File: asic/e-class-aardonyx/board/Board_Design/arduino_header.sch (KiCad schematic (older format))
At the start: 31 parts, among them J10 Conn_1x6_F, J11 Conn_1x6_F, J12 Conn_1x3_M, J13 Conn_1x8_F, J14 Conn_1x6_F, J15 Conn_1x10, J16 Conn_1x8_F, J7 Conn_1x4, J8 Conn_1x3_M, J9 Conn_1x8, U5 CAT24M01WI-GT3, U6 IS25LP256x-xM, U7 ADC108S102CIMTX, U8 LSF0108PWR, U9 LSF0108PWR

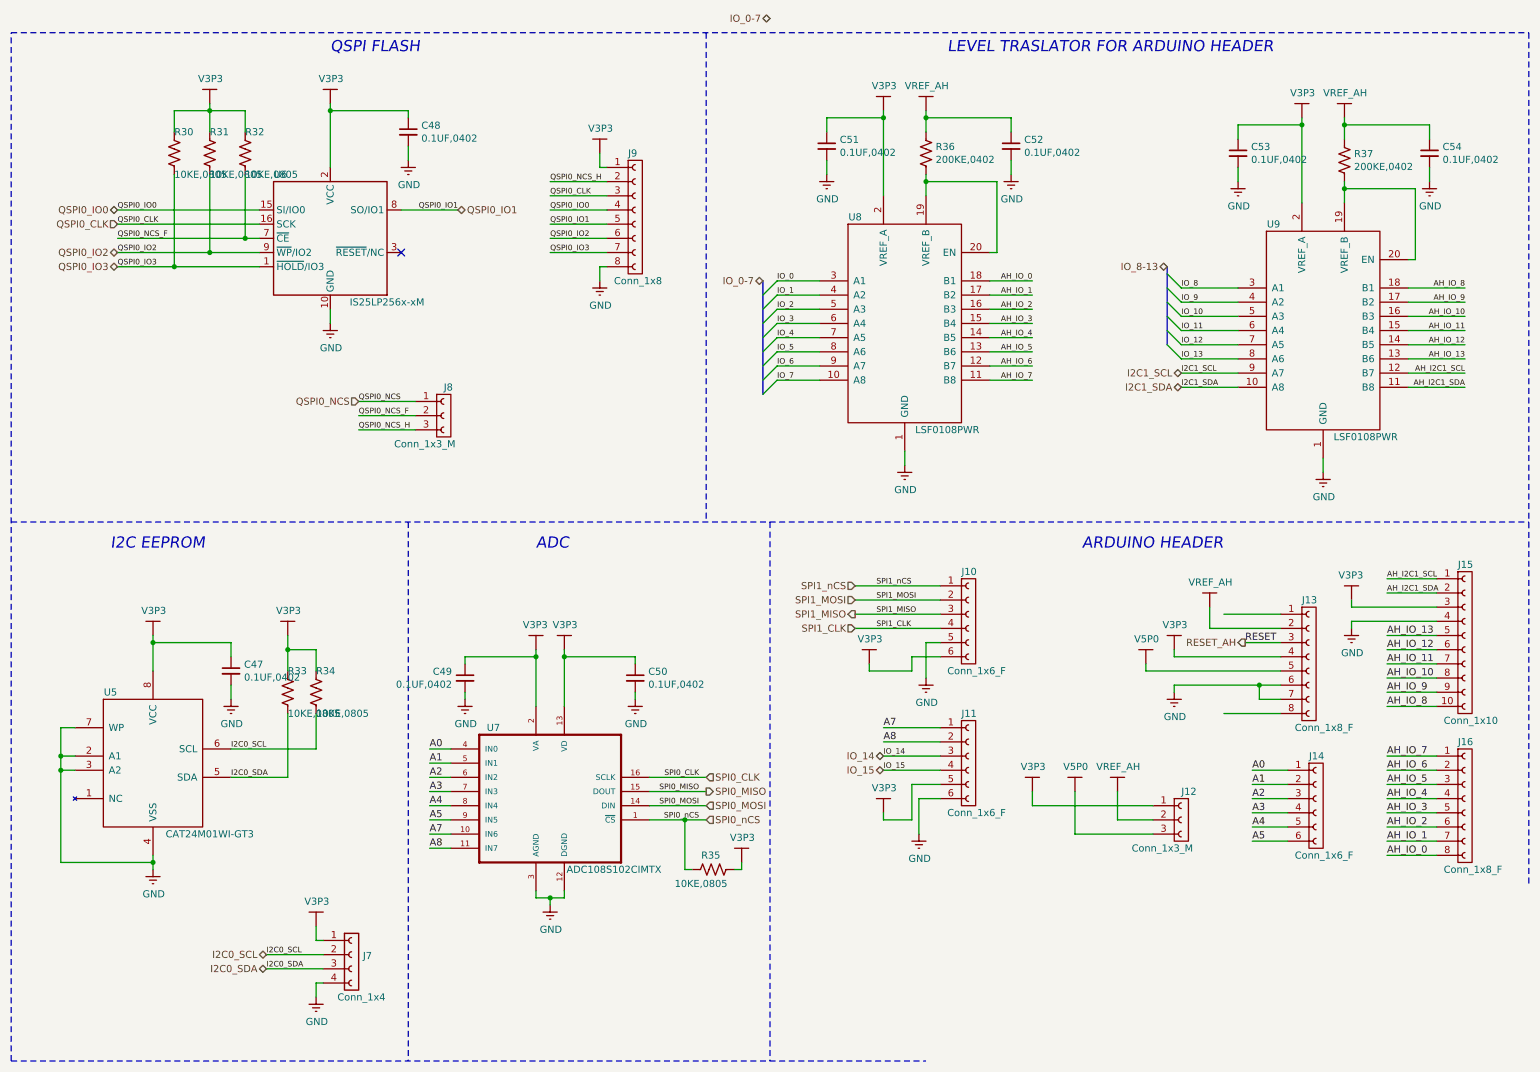
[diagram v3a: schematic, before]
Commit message: updated commented pending schematic
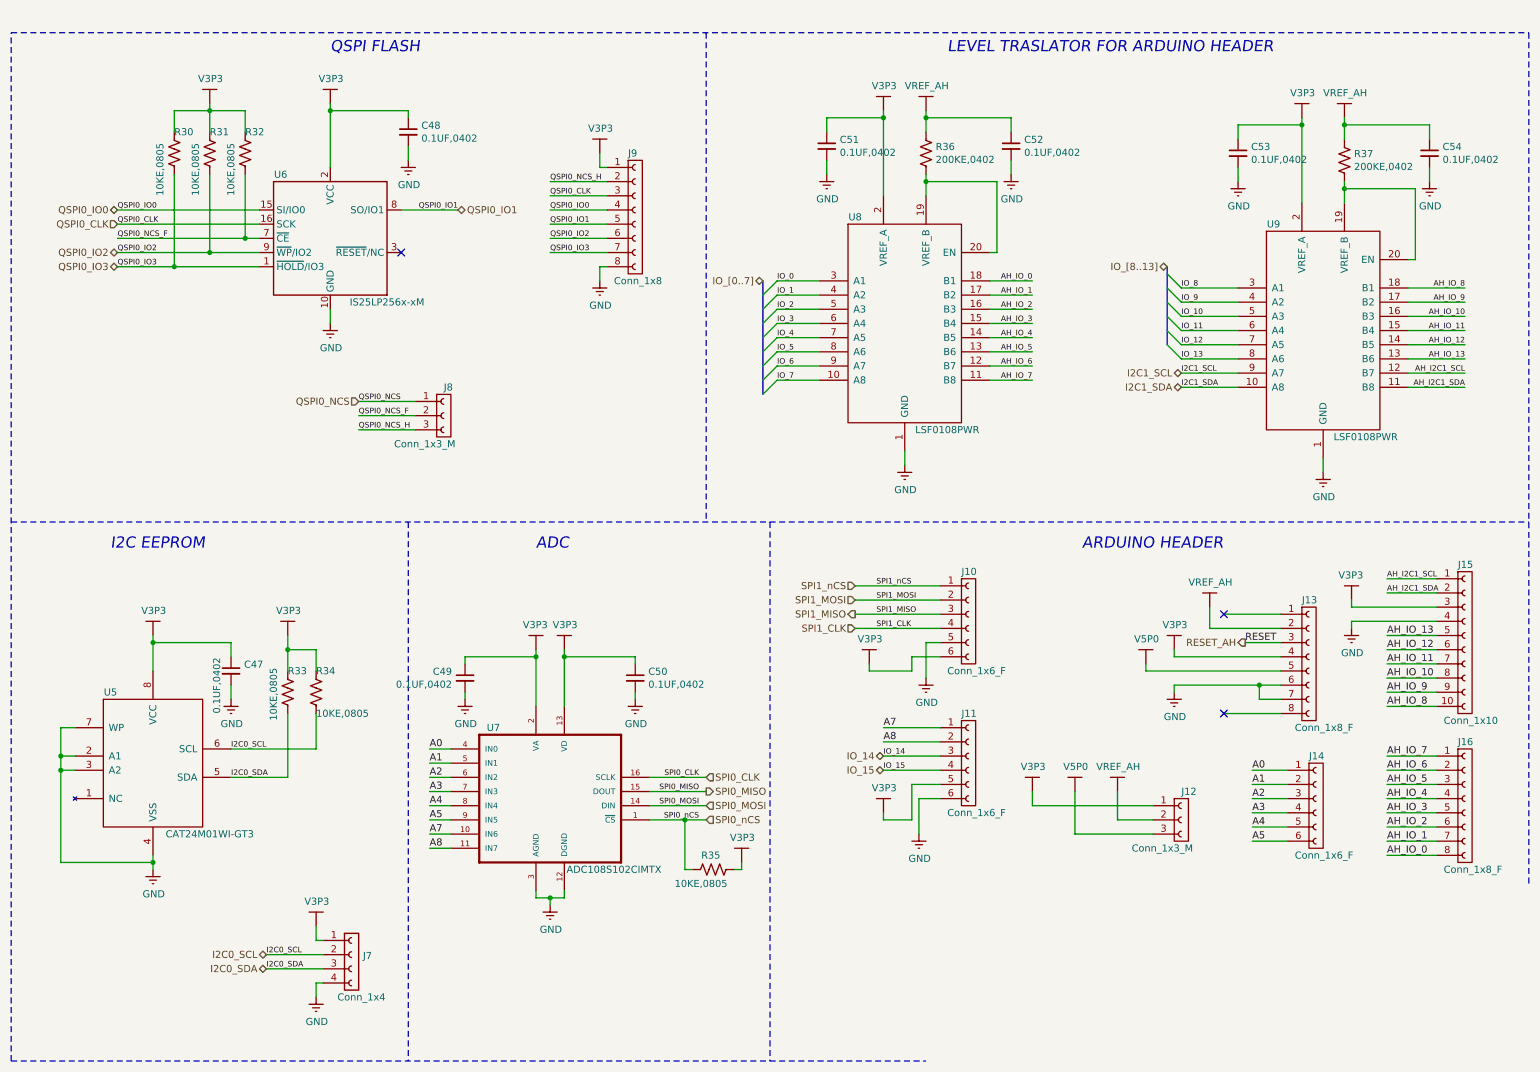
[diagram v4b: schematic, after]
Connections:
- no-connect marks 1 -> 3
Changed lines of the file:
@@
-	1    0    0    -1
-$EndComp
-$Comp
-L Aardonyx-rescue:GND-aardonyx #PWR092
-U 1 1 5E2602C3
-P 10500 1550
-F 0 "#PWR092" H 10500 1300 50  0001 C CNN
-F 1 "GND" H 10505 1377 50  0000 C CNN
-F 2 "" H 10500 1550 50  0001 C CNN
-F 3 "" H 10500 1550 50  0001 C CNN
-	1    10500 1550
 	1    0    0    -1
 $EndComp
@@
 	1    0    0    -1
 $EndComp
-$Comp
-L Aardonyx-rescue:GND-aardonyx #PWR086
-U 1 1 5E266919
-P 9150 1550
-F 0 "#PWR086" H 9150 1300 50  0001 C CNN
-F 1 "GND" H 9155 1377 50  0000 C CNN
-F 2 "" H 9150 1550 50  0001 C CNN
-F 3 "" H 9150 1550 50  0001 C CNN
-	1    9150 1550
-	1    0    0    -1
-$EndComp
 Wire Wire Line
 	9150 1450 9150 1550
@@
 P 2150 1350
 F 0 "R32" H 2150 1500 50  0000 L CNN
-F 1 "10KE,0805" H 2150 1200 50  0000 L CNN
+F 1 "10KE,0805" V 2050 1050 50  0000 L CNN
 F 2 "" V 2190 1340 50  0001 C CNN
 F 3 "https://www.digikey.in/product-detail/en/yageo/RC0805FR-0710KL/311-10-0KCRCT-ND/730482" H 2150 1350 50  0001 C CNN
@@
 P 1650 1350
 F 0 "R30" H 1650 1500 50  0000 L CNN
-F 1 "10KE,0805" H 1650 1200 50  0000 L CNN
+F 1 "10KE,0805" V 1550 1050 50  0000 L CNN
 F 2 "" V 1690 1340 50  0001 C CNN
 F 3 "https://www.digikey.in/product-detail/en/yageo/RC0805FR-0710KL/311-10-0KCRCT-ND/730482" H 1650 1350 50  0001 C CNN
@@
 P 1900 1350
 F 0 "R31" H 1900 1500 50  0000 L CNN
-F 1 "10KE,0805" H 1900 1200 50  0000 L CNN
+F 1 "10KE,0805" V 1800 1050 50  0000 L CNN
 F 2 "" V 1940 1340 50  0001 C CNN
 F 3 "https://www.digikey.in/product-detail/en/yageo/RC0805FR-0710KL/311-10-0KCRCT-ND/730482" H 1900 1350 50  0001 C CNN
@@
 P 2050 5000
 F 0 "C47" H 2142 5046 50  0000 L CNN
-F 1 "0.1UF,0402" H 2142 4955 50  0000 L CNN
+F 1 "0.1UF,0402" V 1950 4700 50  0000 L CNN
 F 2 "" H 2050 5000 50  0001 C CNN
 F 3 "https://www.digikey.in/product-detail/en/avx-corporation/04023C104JAT2A/478-10050-1-ND/6564273" H 2050 5000 50  0001 C CNN
@@
 P 2450 5150
 F 0 "R33" H 2450 5300 50  0000 L CNN
-F 1 "10KE,0805" H 2450 5000 50  0000 L CNN
+F 1 "10KE,0805" V 2350 4950 50  0000 L CNN
 F 2 "" V 2490 5140 50  0001 C CNN
 F 3 "https://www.digikey.in/product-detail/en/yageo/RC0805FR-0710KL/311-10-0KCRCT-ND/730482" H 2450 5150 50  0001 C CNN
@@
 Entry Wire Line
 	5800 3050 5900 2950
-Text HLabel 5850 400  0    50   BiDi ~ 0
-IO_0-7
 Wire Wire Line
 	9150 2300 8750 2300
@@
 	8750 2800 8650 2700
 Text HLabel 8650 2150 0    50   BiDi ~ 0
-IO_8-13
+IO_[8..13]
 Text HLabel 8750 2900 0    50   BiDi ~ 0
 I2C1_SCL
@@
 	10550 5250 10200 5250
 Text HLabel 5800 2250 0    50   BiDi ~ 0
-IO_0-7
+IO_[0..7]
 Text Label 3450 6150 0    50   ~ 0
 A7
@@
 	4200 4850 4200 4900
 Connection ~ 4200 4900
+NoConn ~ 9050 4600
+NoConn ~ 9050 5300
+$Comp
+L Aardonyx-rescue:GND-skt32e_asic #PWR0145
+U 1 1 5EE696CA
+P 9150 1550
+F 0 "#PWR0145" H 9150 1300 50  0001 C CNN
+F 1 "GND" H 9155 1377 50  0000 C CNN
+F 2 "" H 9150 1550 50  0001 C CNN
+F 3 "" H 9150 1550 50  0001 C CNN
+	1    9150 1550
+	1    0    0    -1
+$EndComp
+$Comp
+L Aardonyx-rescue:GND-skt32e_asic #PWR0146
+U 1 1 5EE6C80F
+P 10500 1550
+F 0 "#PWR0146" H 10500 1300 50  0001 C CNN
+F 1 "GND" H 10505 1377 50  0000 C CNN
+F 2 "" H 10500 1550 50  0001 C CNN
+F 3 "" H 10500 1550 50  0001 C CNN
+	1    10500 1550
+	1    0    0    -1
+$EndComp
 Wire Bus Line
 	8650 2150 8650 2700

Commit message: updated footprint for netlist
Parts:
- C47, C48, C49, C50, C51, C52, C53, C54: footprint (none) -> Capacitor_SMD:C_0402_1005Metric
- J12, J8: footprint (none) -> Connector:FanPinHeader_1x03_P2.54mm_Vertical
- R30, R31, R32, R33, R34, R35: footprint (none) -> Resistor_SMD:R_0805_2012Metric
- R36, R37: footprint (none) -> Resistor_SMD:R_0402_1005Metric
- U5: footprint (none) -> Package_SO:TSSOP-8_4.4x3mm_P0.65mm
- U7: footprint (none) -> Package_SO:TSSOP-16_4.4x5mm_P0.65mm
- U8, U9: footprint (none) -> Package_SO:TSSOP-20_4.4x6.5mm_P0.65mm
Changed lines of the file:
@@
 EESchema Schematic File Version 4
-LIBS:Aardonyx-cache
-EELAYER 29 0
+EELAYER 30 0
 EELAYER END
 $Descr A4 11693 8268
@@
 F 0 "U5" H 1200 6150 50  0000 C CNN
 F 1 "CAT24M01WI-GT3" H 1900 5150 50  0000 C CNN
-F 2 "" H 1500 5650 50  0001 C CNN
+F 2 "Package_SO:TSSOP-8_4.4x3mm_P0.65mm" H 1500 5650 50  0001 C CNN
 F 3 "https://www.digikey.in/product-detail/en/on-semiconductor/CAT24M01WI-GT3/CAT24M01WI-GT3OSCT-ND/2698362" H 1500 5650 50  0001 C CNN
 F 4 "IC EEPROM 1M I2C 1MHZ 8SOIC" H 1500 5650 50  0001 C CNN "Description"
@@
 F 0 "U9" H 9400 3350 50  0000 C CNN
 F 1 "LSF0108PWR" H 10050 1850 50  0000 C CNN
-F 2 "" H 9750 2600 50  0001 C CNN
+F 2 "Package_SO:TSSOP-20_4.4x6.5mm_P0.65mm" H 9750 2600 50  0001 C CNN
 F 3 "https://www.digikey.in/product-detail/en/texas-instruments/LSF0108PWR/296-37828-1-ND/4876357" H 9750 2600 50  0001 C CNN
 F 4 "IC TRNSLTR BIDIRECTIONAL 20TSSOP" H 9750 2600 50  0001 C CNN "Description"
@@
 F 0 "R36" H 7018 1396 50  0000 L CNN
 F 1 "200KE,0402" H 7018 1305 50  0000 L CNN
-F 2 "" V 6990 1340 50  0001 C CNN
+F 2 "Resistor_SMD:R_0402_1005Metric" V 6990 1340 50  0001 C CNN
 F 3 "https://www.digikey.com/product-detail/en/koa-speer-electronics-inc/RN73H1ETTP2003B25/2019-RN73H1ETTP2003B25CT-ND/9916930" H 6950 1350 50  0001 C CNN
 F 4 " RES 200K OHM 0.1% 1/16W 0402 " H 6950 1350 50  0001 C CNN "Description"
@@
 F 0 "C52" H 7642 1346 50  0000 L CNN
 F 1 "0.1UF,0402" H 7642 1255 50  0000 L CNN
-F 2 "" H 7550 1300 50  0001 C CNN
+F 2 "Capacitor_SMD:C_0402_1005Metric" H 7550 1300 50  0001 C CNN
 F 3 "https://www.digikey.in/product-detail/en/avx-corporation/04023C104JAT2A/478-10050-1-ND/6564273" H 7550 1300 50  0001 C CNN
 F 4 "CAP CER 0.1UF 25V X7R 0402" H 7550 1300 50  0001 C CNN "Description"
@@
 F 0 "R37" H 9968 1446 50  0000 L CNN
 F 1 "200KE,0402" H 9968 1355 50  0000 L CNN
-F 2 "" V 9940 1390 50  0001 C CNN
+F 2 "Resistor_SMD:R_0402_1005Metric" V 9940 1390 50  0001 C CNN
 F 3 "https://www.digikey.com/product-detail/en/koa-speer-electronics-inc/RN73H1ETTP2003B25/2019-RN73H1ETTP2003B25CT-ND/9916930" H 9900 1400 50  0001 C CNN
 F 4 " RES 200K OHM 0.1% 1/16W 0402 " H 9900 1400 50  0001 C CNN "Description"
@@
 F 0 "C53" H 9242 1396 50  0000 L CNN
 F 1 "0.1UF,0402" H 9242 1305 50  0000 L CNN
-F 2 "" H 9150 1350 50  0001 C CNN
+F 2 "Capacitor_SMD:C_0402_1005Metric" H 9150 1350 50  0001 C CNN
 F 3 "https://www.digikey.in/product-detail/en/avx-corporation/04023C104JAT2A/478-10050-1-ND/6564273" H 9150 1350 50  0001 C CNN
 F 4 "CAP CER 0.1UF 25V X7R 0402" H 9150 1350 50  0001 C CNN "Description"
@@
 F 0 "C51" H 6342 1346 50  0000 L CNN
 F 1 "0.1UF,0402" H 6342 1255 50  0000 L CNN
-F 2 "" H 6250 1300 50  0001 C CNN
+F 2 "Capacitor_SMD:C_0402_1005Metric" H 6250 1300 50  0001 C CNN
 F 3 "https://www.digikey.in/product-detail/en/avx-corporation/04023C104JAT2A/478-10050-1-ND/6564273" H 6250 1300 50  0001 C CNN
 F 4 "CAP CER 0.1UF 25V X7R 0402" H 6250 1300 50  0001 C CNN "Description"
@@
 F 0 "U8" H 6450 3300 50  0000 C CNN
 F 1 "LSF0108PWR" H 7100 1800 50  0000 C CNN
-F 2 "" H 6800 2550 50  0001 C CNN
+F 2 "Package_SO:TSSOP-20_4.4x6.5mm_P0.65mm" H 6800 2550 50  0001 C CNN
 F 3 "https://www.digikey.in/product-detail/en/texas-instruments/LSF0108PWR/296-37828-1-ND/4876357" H 6800 2550 50  0001 C CNN
 F 4 "IC TRNSLTR BIDIRECTIONAL 20TSSOP" H 6800 2550 50  0001 C CNN "Description"
@@
 F 0 "C54" H 10592 1396 50  0000 L CNN
 F 1 "0.1UF,0402" H 10592 1305 50  0000 L CNN
-F 2 "" H 10500 1350 50  0001 C CNN
+F 2 "Capacitor_SMD:C_0402_1005Metric" H 10500 1350 50  0001 C CNN
 F 3 "https://www.digikey.in/product-detail/en/avx-corporation/04023C104JAT2A/478-10050-1-ND/6564273" H 10500 1350 50  0001 C CNN
 F 4 "CAP CER 0.1UF 25V X7R 0402" H 10500 1350 50  0001 C CNN "Description"
@@
 F 0 "C48" H 3392 1246 50  0000 L CNN
 F 1 "0.1UF,0402" H 3392 1155 50  0000 L CNN
-F 2 "" H 3300 1200 50  0001 C CNN
+F 2 "Capacitor_SMD:C_0402_1005Metric" H 3300 1200 50  0001 C CNN
 F 3 "https://www.digikey.in/product-detail/en/avx-corporation/04023C104JAT2A/478-10050-1-ND/6564273" H 3300 1200 50  0001 C CNN
 F 4 "CAP CER 0.1UF 25V X7R 0402" H 3300 1200 50  0001 C CNN "Description"
@@
 F 0 "R32" H 2150 1500 50  0000 L CNN
 F 1 "10KE,0805" V 2050 1050 50  0000 L CNN
-F 2 "" V 2190 1340 50  0001 C CNN
+F 2 "Resistor_SMD:R_0805_2012Metric" V 2190 1340 50  0001 C CNN
 F 3 "https://www.digikey.in/product-detail/en/yageo/RC0805FR-0710KL/311-10-0KCRCT-ND/730482" H 2150 1350 50  0001 C CNN
 F 4 "RES SMD 10K OHM 1% 1/8W 0805" H 2150 1350 50  0001 C CNN "Description"
@@
 F 0 "R30" H 1650 1500 50  0000 L CNN
 F 1 "10KE,0805" V 1550 1050 50  0000 L CNN
-F 2 "" V 1690 1340 50  0001 C CNN
+F 2 "Resistor_SMD:R_0805_2012Metric" V 1690 1340 50  0001 C CNN
 F 3 "https://www.digikey.in/product-detail/en/yageo/RC0805FR-0710KL/311-10-0KCRCT-ND/730482" H 1650 1350 50  0001 C CNN
 F 4 "RES SMD 10K OHM 1% 1/8W 0805" H 1650 1350 50  0001 C CNN "Description"
@@
 F 0 "R31" H 1900 1500 50  0000 L CNN
 F 1 "10KE,0805" V 1800 1050 50  0000 L CNN
-F 2 "" V 1940 1340 50  0001 C CNN
+F 2 "Resistor_SMD:R_0805_2012Metric" V 1940 1340 50  0001 C CNN
 F 3 "https://www.digikey.in/product-detail/en/yageo/RC0805FR-0710KL/311-10-0KCRCT-ND/730482" H 1900 1350 50  0001 C CNN
 F 4 "RES SMD 10K OHM 1% 1/8W 0805" H 1900 1350 50  0001 C CNN "Description"
@@
 F 0 "C47" H 2142 5046 50  0000 L CNN
 F 1 "0.1UF,0402" V 1950 4700 50  0000 L CNN
-F 2 "" H 2050 5000 50  0001 C CNN
+F 2 "Capacitor_SMD:C_0402_1005Metric" H 2050 5000 50  0001 C CNN
 F 3 "https://www.digikey.in/product-detail/en/avx-corporation/04023C104JAT2A/478-10050-1-ND/6564273" H 2050 5000 50  0001 C CNN
 F 4 "CAP CER 0.1UF 25V X7R 0402" H 2050 5000 50  0001 C CNN "Description"
@@
 F 0 "R33" H 2450 5300 50  0000 L CNN
 F 1 "10KE,0805" V 2350 4950 50  0000 L CNN
-F 2 "" V 2490 5140 50  0001 C CNN
+F 2 "Resistor_SMD:R_0805_2012Metric" V 2490 5140 50  0001 C CNN
 F 3 "https://www.digikey.in/product-detail/en/yageo/RC0805FR-0710KL/311-10-0KCRCT-ND/730482" H 2450 5150 50  0001 C CNN
 F 4 "RES SMD 10K OHM 1% 1/8W 0805" H 2450 5150 50  0001 C CNN "Description"
@@
 F 0 "R34" H 2650 5300 50  0000 L CNN
 F 1 "10KE,0805" H 2650 5000 50  0000 L CNN
-F 2 "" V 2690 5140 50  0001 C CNN
+F 2 "Resistor_SMD:R_0805_2012Metric" V 2690 5140 50  0001 C CNN
 F 3 "https://www.digikey.in/product-detail/en/yageo/RC0805FR-0710KL/311-10-0KCRCT-ND/730482" H 2650 5150 50  0001 C CNN
 F 4 "RES SMD 10K OHM 1% 1/8W 0805" H 2650 5150 50  0001 C CNN "Description"
@@
 F 0 "J12" H 8750 6250 50  0000 L CNN
 F 1 "Conn_1x3_M" H 8400 5850 50  0000 L CNN
-F 2 "" H 8750 6050 50  0001 C CNN
+F 2 "Connector:FanPinHeader_1x03_P2.54mm_Vertical" H 8750 6050 50  0001 C CNN
 F 3 "https://www.digikey.com/product-detail/en/amphenol-icc-fci/68000-203HLF/609-3464-ND/2023305" H 8750 6050 50  0001 C CNN
 F 4 "CONN HEADER VERT 3POS 2.54MM" H 8750 6050 50  0001 C CNN "Description"
@@
 F 0 "C50" H 4992 5096 50  0000 L CNN
 F 1 "0.1UF,0402" H 4992 5005 50  0000 L CNN
-F 2 "" H 4900 5050 50  0001 C CNN
+F 2 "Capacitor_SMD:C_0402_1005Metric" H 4900 5050 50  0001 C CNN
 F 3 "https://www.digikey.in/product-detail/en/avx-corporation/04023C104JAT2A/478-10050-1-ND/6564273" H 4900 5050 50  0001 C CNN
 F 4 "CAP CER 0.1UF 25V X7R 0402" H 4900 5050 50  0001 C CNN "Description"
@@
 F 0 "R35" V 5550 6350 50  0000 L CNN
 F 1 "10KE,0805" V 5350 6300 50  0000 L CNN
-F 2 "" V 5490 6390 50  0001 C CNN
+F 2 "Resistor_SMD:R_0805_2012Metric" V 5490 6390 50  0001 C CNN
 F 3 "https://www.digikey.in/product-detail/en/yageo/RC0805FR-0710KL/311-10-0KCRCT-ND/730482" H 5450 6400 50  0001 C CNN
 F 4 "RES SMD 10K OHM 1% 1/8W 0805" H 5450 6400 50  0001 C CNN "Description"
@@
 F 0 "C49" H 3792 5096 50  0000 L CNN
 F 1 "0.1UF,0402" H 3792 5005 50  0000 L CNN
-F 2 "" H 3700 5050 50  0001 C CNN
+F 2 "Capacitor_SMD:C_0402_1005Metric" H 3700 5050 50  0001 C CNN
 F 3 "https://www.digikey.in/product-detail/en/avx-corporation/04023C104JAT2A/478-10050-1-ND/6564273" H 3700 5050 50  0001 C CNN
 F 4 "CAP CER 0.1UF 25V X7R 0402" H 3700 5050 50  0001 C CNN "Description"
@@
 F 0 "J8" H 3550 3400 50  0000 L CNN
 F 1 "Conn_1x3_M" H 3200 3000 50  0000 L CNN
-F 2 "" H 3550 3200 50  0001 C CNN
+F 2 "Connector:FanPinHeader_1x03_P2.54mm_Vertical" H 3550 3200 50  0001 C CNN
 F 3 "https://www.digikey.com/product-detail/en/amphenol-icc-fci/68000-203HLF/609-3464-ND/2023305" H 3550 3200 50  0001 C CNN
 F 4 "CONN HEADER VERT 3POS 2.54MM" H 3550 3200 50  0001 C CNN "Description"
@@
 F 0 "U7" H 3900 6400 50  0000 C CNN
 F 1 "ADC108S102CIMTX" H 4750 5400 50  0000 C CNN
-F 2 "" H 4300 5900 50  0001 L BNN
+F 2 "Package_SO:TSSOP-16_4.4x5mm_P0.65mm" H 4300 5900 50  0001 L BNN
 F 3 "https://www.digikey.in/product-detail/en/texas-instruments/ADC108S102CIMTX-NOPB/296-43835-1-ND/5875706" H 4300 5900 50  0001 L BNN
 F 4 "ADC108S102CIMTX/NOPB" H 4300 5900 50  0001 C CNN "Description"
